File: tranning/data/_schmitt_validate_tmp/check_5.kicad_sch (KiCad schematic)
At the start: 1 part, among them U1 74HC14

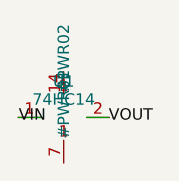
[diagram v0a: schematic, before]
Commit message: Fix overlapping and mis-wired schematics; add ESP32, Mega 2560, Pi 5
- circuit_rule_check.transform_point: flip the library y axis. Verified
  against KiCad's own demo schematics (42/42 and 182/182 pins on a wire);
  the old formula made generated files open in KiCad with +5V on the GND
  pin and the reset pull-up on PB0.
- circuit_ic_generator: rewritten layout. IC pins get a short stub to an
  outward-facing power symbol or a net label; decoupling, reset and
  crystal circuits are measured blocks stacked beside the IC, checked for
  overlap before writing; drawing placed on an auto-sized page; library
  symbols get graphics. Adds ESP32-WROOM-32, ATmega2560, Pi 5 header.
- circuit_rule_check: same-name nets are joined (KiCad behaviour), new
  overlapping_symbols rule, 3V3/EN pin names recognised.
- circuit_kicad_to_schemdraw: draws labels, power flags and IC pin names;
  pin side taken from the pin's own direction.
- schmitt_trigger_gen: library block fixed so KiCad wires IN+/IN- and
  V+/V- as intended and power pins join GND/VCC; model output unchanged.
- Tests: 65 pass, including a real kicad-cli netlist check.

Co-Authored-By: Claude Opus 5.5 <noreply@anthropic.com>
Claude-Session: https://claude.ai/code/session_01TWSKnHncRvWd1K9A45SkP5
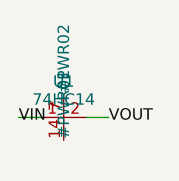
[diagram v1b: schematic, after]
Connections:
- net VCC: now reaches U1.14
- net GND: now reaches U1.7

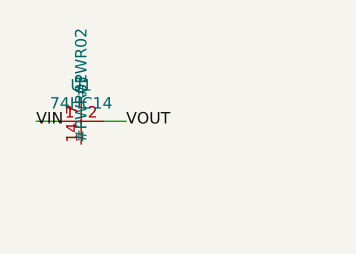
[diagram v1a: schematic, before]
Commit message: Redesign Schmitt-trigger templates without overlaps (retrain in progress)
- schmitt_trigger_gen: KiCad-sized op-amp/resistor/inverter symbols with
  graphics; every pin position computed with transform_point; orthogonal
  wiring with the feedback resistor routed above/below the op-amp; labels
  and power-net names placed away from parts; power references hidden.
  uuids are added by wrap_kicad() instead of the model (~90 tokens less
  per circuit), so the longest pair is 990 tokens (block_size 1024).
  validate_pairs now rejects overlap warnings too.
- circuit_rule_check: a multi-pin part's body is where its pins end (tip
  plus pin length), so supply symbols on an op-amp's V+/V- tips are not
  counted as overlapping it.
- schmitt_trigger_train: --checkpoint-every (default 10) for long runs.
- Tests: real-KiCad netlist check for four topologies; context-length check.

The checked-in schmitt model still matches the old templates until the
retrain running now finishes.

Co-Authored-By: Claude Opus 5.5 <noreply@anthropic.com>
Claude-Session: https://claude.ai/code/session_01TWSKnHncRvWd1K9A45SkP5
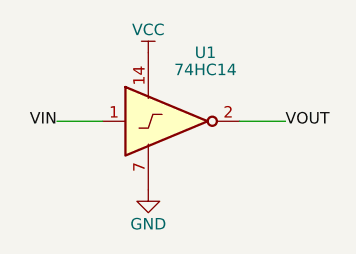
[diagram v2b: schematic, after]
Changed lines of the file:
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@@
 (kicad_sch (version 20231120) (generator sinco_schmitt_gen) (paper "A4")
- (symbol (lib_id "Sinco:SchmittInverter") (at 100.0 100.0 0) (unit 1)(property "Reference" "U1" (at 100.0 96.0 0)) (property "Value" "74HC14" (at 100.0 98.0 0)))(symbol (lib_id "power:VCC") (at 100.0 102.54 90) (unit 1)(property "Reference" "#PWR01" (at 100.0 98.54 0)) )(symbol (lib_id "power:GND") (at 100.0 97.46 90) (unit 1)(property "Reference" "#PWR02" (at 100.0 93.46 0)) )(wire (pts (xy 95.0 100.0) (xy 97.46 100.0)))(wire (pts (xy 102.54 100.0) (xy 105.0 100.0)))(label "VIN" (at 95.0 100.0 0))(label "VOUT" (at 105.0 100.0 0)))
+ (symbol (lib_id "Sinco:SchmittInverter") (at 110.0 100.0 0) (unit 1) (property "Reference" "U1" (at 113.81 92.38 0)) (property "Value" "74HC14" (at 113.81 94.285 0)))(symbol (lib_id "power:VCC") (at 107.46 92.38 0) (unit 1) (property "Reference" "#PWR01" (at 107.46 88.316 0) (effects hide)) (property "Value" "VCC" (at 107.46 89.83999999999999 0)))(symbol (lib_id "power:GND") (at 107.46 107.62 0) (unit 1) (property "Reference" "#PWR02" (at 107.46 103.55600000000001 0) (effects hide)) (property "Value" "GND" (at 107.46 111.43 0)))(wire (pts (xy 97.3 100.0) (xy 102.38 100.0)))(wire (pts (xy 117.62 100.0) (xy 122.7 100.0)))(label "VIN" (at 97.3 100.0 180))(label "VOUT" (at 122.7 100.0 0)))
